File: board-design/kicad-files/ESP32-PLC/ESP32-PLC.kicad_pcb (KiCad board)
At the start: 2 copper layers, 58.1 x 172.1 mm, 80 parts, among them J1 640456-3, J2 Conn_ARM_JTAG_SWD_10, J3 302-S101, J4 302-S101, J5 RJ45_Wuerth_7499010121A, Q1 BC817, Q2 BC817, U1 BD48ExxG, U2 ESP32-WROVER-E, U3 LAN8720A, Y1 Q25MHz/20ppm/3.2x2.5mm (FL250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

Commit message: [UPDATE]
Finished ESP32 and ESP32-programmer board designs (few corrections to be made when manufacturer is chosen - design rules).

Signed-off-by: Nicolae-Andrei Vasile <vasilenicolaeandrei@gmail.com>
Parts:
- added H1: MountingHole, MountingHole:MountingHole_2.5mm_Pad_Via, F.Cu at (73.9, 24.1)
- added H2: MountingHole, MountingHole:MountingHole_2.5mm_Pad_Via, F.Cu at (123.9, 24.1)
- added H3: MountingHole, MountingHole:MountingHole_2.5mm_Pad_Via, F.Cu at (73.9, 186.1)
- added H4: MountingHole, MountingHole:MountingHole_2.5mm_Pad_Via, F.Cu at (123.9, 186.1)
- J4: moved to B.Cu
- moved R19 186.2 mm to (83.8, 144.1)
- moved R20 186.2 mm to (83.8, 145.4)
- moved R13 177.1 mm to (83.8, 153.0)
- moved R14 177.0 mm to (83.8, 154.3)
- moved R15 176.5 mm to (83.8, 151.8)
- moved U2 142.7 mm to (107.6, 63.9), turned to -90 degrees
- moved C6 122.3 mm to (115.6, 52.7), turned to 0 degrees
- moved C7 120.2 mm to (115.6, 50.8), turned to 0 degrees
- moved R1 115.6 mm to (107.3, 47.0), turned to -90 degrees
- moved J4 114.0 mm to (94.0, 24.6), turned to -90 degrees
- moved C8 113.4 mm to (117.5, 47.0), turned to 0 degrees
- moved C24 112.8 mm to (104.8, 138.4)
- moved L3 107.5 mm to (104.8, 136.5)
- moved R5 106.9 mm to (100.8, 42.5), turned to 180 degrees
- moved J3 106.7 mm to (94.0, 87.1), turned to 90 degrees
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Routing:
- net Net-(U3-VDD1A): track 0.00 -> 192.1 mm, vias 0 -> 9
- net +3V3: track 0.00 -> 181.6 mm, vias 0 -> 2
- net /LAN8720A/GPIO26/EMAC_RXD1: track 0.00 -> 151.5 mm, vias 0 -> 2
- net /LAN8720A/GPIO25/EMAC_RXD0: track 0.00 -> 149.6 mm, vias 0 -> 2
- net /GPIO0/REFCLKO: track 0.00 -> 139.7 mm, vias 0 -> 3
- net Net-(Q1-C): track 0.00 -> 137.0 mm, vias 0 -> 2
- net /LAN8720A/GPIO22/EMAC_TXD1: track 0.00 -> 135.2 mm, vias 0 -> 2
- net /LAN8720A/GPIO5/~{RST}: track 0.00 -> 126.0 mm, vias 0 -> 2
- net /LAN8720A/GPIO19/EMAC_TXD0: track 0.00 -> 123.7 mm, vias 0 -> 2
- net /LAN8720A/GPIO27/EMAC_CRS_DV: track 0.00 -> 123.6 mm, vias 0 -> 2
- net /LAN8720A/GPIO23/MDC: track 0.00 -> 122.8 mm, vias 0 -> 2
- net Net-(U1-VDD): track 0.00 -> 120.3 mm, vias 0 -> 2
- net /LAN8720A/GPIO21/EMAC_TXEN: track 0.00 -> 120.2 mm, vias 0 -> 2
- net /LAN8720A/GPIO18/MDIO: track 0.00 -> 107.2 mm, vias 0 -> 2
- net /ESP32_INT: track 0.00 -> 100.1 mm, vias 0 -> 1
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- added copper zone on B.Cu, net Earth_Protective
- added copper zone on F.Cu, net Earth_Protective
- added copper zone on B.Cu, net GND
- added copper zone on F.Cu, net GND

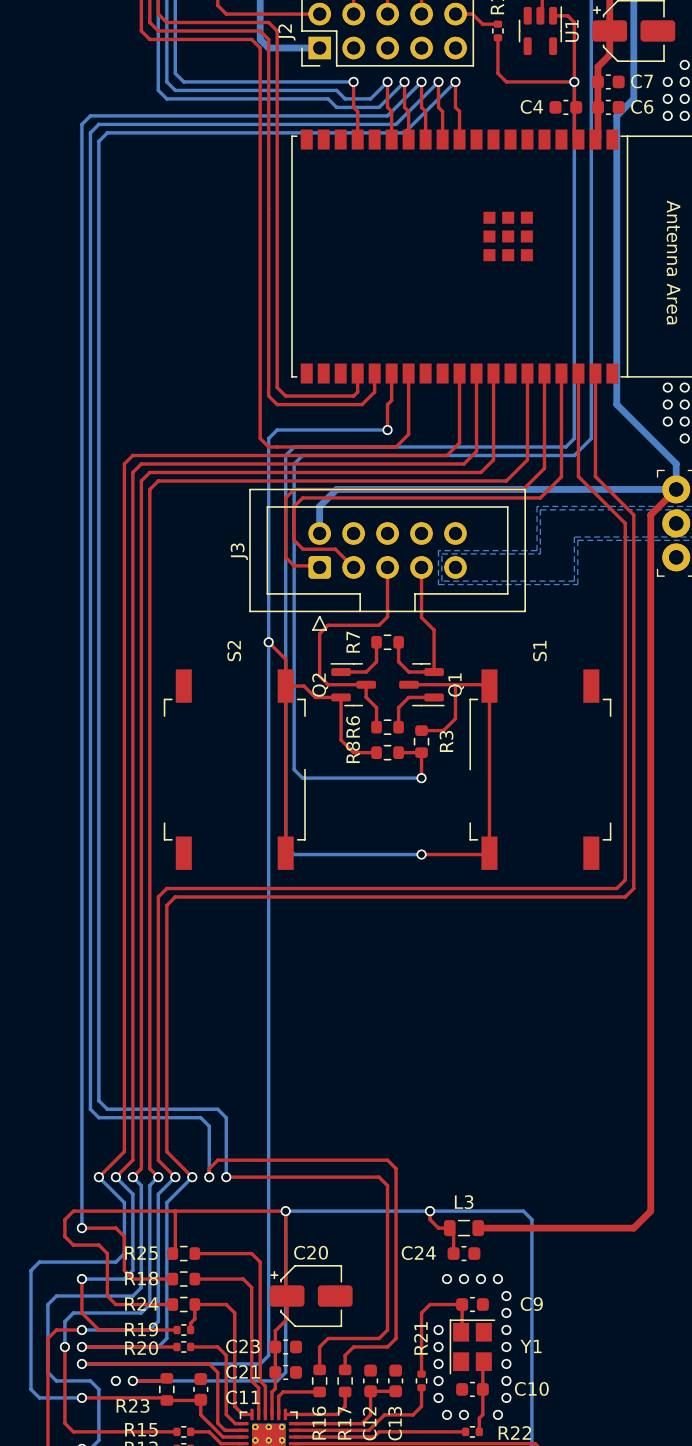
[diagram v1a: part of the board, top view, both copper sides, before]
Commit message: [FIX]
Updated footprints for tactile switches.

Signed-off-by: Nicolae-Andrei Vasile <vasilenicolaeandrei@gmail.com>
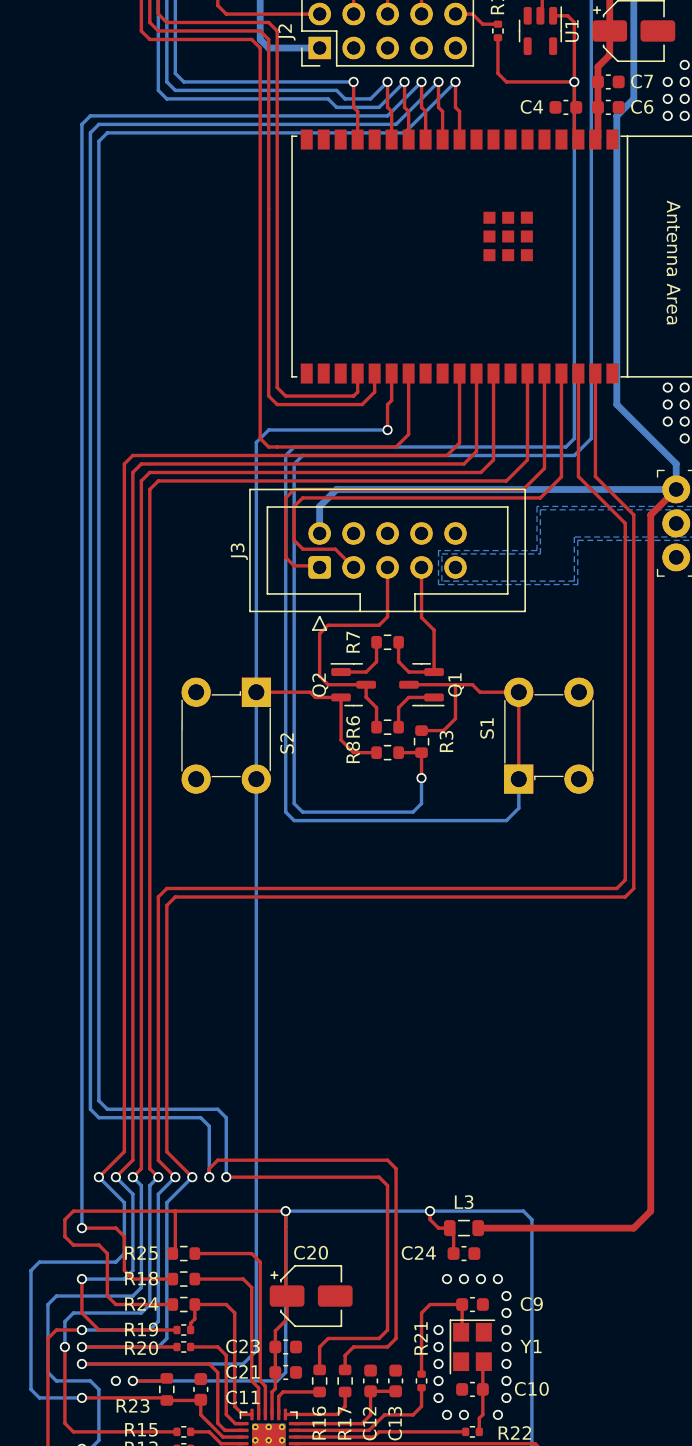
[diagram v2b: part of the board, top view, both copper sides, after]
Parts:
- S1, S2: footprint Button_Switch_SMD:SW_MEC_5GSH9 -> digikey-footprints:Switch_Tactile_THT_6x6mm
- moved S2 6.01 mm to (89.2, 96.4), turned to -90 degrees
- moved S1 1.76 mm to (108.9, 102.9), turned to 90 degrees
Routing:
- net /GPIO0/REFCLKO: track 139.7 -> 125.0 mm, vias 3 -> 2
- net Net-(U1-VDD): track 120.3 -> 125.1 mm
- net Net-(Q1-C): track 137.0 -> 135.5 mm, vias 2 -> 1

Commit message: [UPDATE]
Work in progress.

Signed-off-by: Nicolae-Andrei Vasile <vasilenicolaeandrei@gmail.com>
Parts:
- added BT1: CR2032 (Panasonic vertical), Battery:Battery_Panasonic_CR2032-VS1N_Vertical_CircularHoles, F.Cu at (96.8, 243.7)
- added C25: 0.1uF/6.3V/20%/C0603, Capacitor_SMD:C_0603_1608Metric, F.Cu at (346.7, 293.4)
- added C26: 33pF/6.3V/20%/C0603, Capacitor_SMD:C_0603_1608Metric, F.Cu at (339.1, 286.4)
- added C27: 33pF/6.3V/20%/C0603, Capacitor_SMD:C_0603_1608Metric, F.Cu at (339.1, 291.5)
- added C28: 10nF/6.3V/20%/C0603, Capacitor_SMD:C_0603_1608Metric, F.Cu at (346.7, 278.1)
- added C29: 33pF/6.3V/20%/C0603, Capacitor_SMD:C_0603_1608Metric, F.Cu at (342.9, 293.4)
- added C30: 100uF/16V/20%/4x5.4mm, Capacitor_SMD:CP_Elec_4x5.4, F.Cu at (373.4, 234.9)
- added C31: 0.1uF/6.3V/20%/C0603, Capacitor_SMD:C_0603_1608Metric, F.Cu at (371.5, 238.8)
- added C32: 33pF/6.3V/20%/C0603, Capacitor_SMD:C_0603_1608Metric, F.Cu at (371.5, 240.7)
- added C33: 10pF/6.3V/20%/C0603, Capacitor_SMD:C_0603_1608Metric, F.Cu at (371.5, 242.6)
- added C34: 10pF/6.3V/20%/C0603, Capacitor_SMD:C_0603_1608Metric, F.Cu at (368.3, 242.6)
- added C35: 33pF/6.3V/20%/C0603, Capacitor_SMD:C_0603_1608Metric, F.Cu at (368.3, 240.7)
- added C36: 0.1uF/6.3V/20%/C0603, Capacitor_SMD:C_0603_1608Metric, F.Cu at (368.3, 238.8)
- added C37: 100uF/16V/20%/4x5.4mm, Capacitor_SMD:CP_Elec_4x5.4, F.Cu at (366.4, 234.9)
- added C38: 1uF/6.3V/20%/C0603, Capacitor_SMD:C_0603_1608Metric, F.Cu at (347.3, 236.9)
- added C39: 1uF/6.3V/20%/C0603, Capacitor_SMD:C_0603_1608Metric, F.Cu at (339.1, 272.4)
- added C40: 10uF/6.3V/20%/C0603, Capacitor_SMD:C_0603_1608Metric, F.Cu at (349.2, 236.9)
- added C41: 10uF/6.3V/20%/C0603, Capacitor_SMD:C_0603_1608Metric, F.Cu at (339.1, 270.5)
- added C42: 0.1uF/6.3V/20%/C0603, Capacitor_SMD:C_0603_1608Metric, F.Cu at (351.2, 236.9)
- added C43: 0.1uF/6.3V/20%/C0603, Capacitor_SMD:C_0603_1608Metric, F.Cu at (339.1, 268.6)
- added C44: 0.1uF/6.3V/20%/C0603, Capacitor_SMD:C_0603_1608Metric, F.Cu at (349.2, 233.0)
- added C45: 0.1uF/6.3V/20%/C0603, Capacitor_SMD:C_0603_1608Metric, F.Cu at (335.3, 270.5)
- added C46: 10uF/6.3V/20%/C0603, Capacitor_SMD:C_0603_1608Metric, F.Cu at (351.2, 233.0)
- added C47: 10uF/6.3V/20%/C0603, Capacitor_SMD:C_0603_1608Metric, F.Cu at (335.3, 268.6)
- added C48: 22uF/6.3V/20%/C0603, Capacitor_SMD:C_0603_1608Metric, F.Cu at (339.1, 254.0)
- added C49: 22uF/6.3V/20%/C0603, Capacitor_SMD:C_0603_1608Metric, F.Cu at (92.8, 246.9)
- added C50: 0.1uF/6.3V/20%/C0603, Capacitor_SMD:C_0603_1608Metric, F.Cu at (92.8, 249.5)
- added C51: 10uF/16V/20%/4x5.4mm, Capacitor_SMD:CP_Elec_4x5.4, F.Cu at (107.2, 248.6)
- added C52: 0.1uF/6.3V/20%/C0603, Capacitor_SMD:C_0603_1608Metric, F.Cu at (92.8, 252.0)
- added C53: 10pF/6.3V/10%/C0603, Capacitor_SMD:C_0603_1608Metric, F.Cu at (92.8, 254.5)
- added C54: 10pF/6.3V/10%/C0603, Capacitor_SMD:C_0603_1608Metric, F.Cu at (92.8, 257.0)
- added C55: 0.1uF/6.3V/20%/C0603, Capacitor_SMD:C_0603_1608Metric, F.Cu at (92.8, 259.5)
- added C56: 10uF/16V/20%/4x5.4mm, Capacitor_SMD:CP_Elec_4x5.4, F.Cu at (107.2, 254.5)
- added D1: ESDA6V1-5SC6, Package_TO_SOT_SMD:SOT-23-6, F.Cu at (342.9, 288.9)
- added D2: VESD05C1-02V, Diode_SMD:D_SOD-523, F.Cu at (373.4, 229.2)
- added D3: 20V/0.5A/0.5V (NSR0620P2T5G), Diode_SMD:D_SOD-923, F.Cu at (101.3, 259.6)
- added J6: RJ45_Wuerth_7499010121A, Connector_RJ:RJ45_Wuerth_7499010121A_Horizontal, F.Cu at (365.2, 55.6)
- added J7: SF53S006VCBR2000, Connector_Card:microSIM_JAE_SF53S006VCBR2000, F.Cu at (355.6, 287.7)
- added L4: FB0805/600R/2A, Inductor_SMD:L_0805_2012Metric, F.Cu at (371.5, 229.2)
- added L5: FB0805/600R/2A, Inductor_SMD:L_0805_2012Metric, F.Cu at (347.3, 233.0)
- added L6: FB0805/600R/2A, Inductor_SMD:L_0805_2012Metric, F.Cu at (335.3, 272.4)
- added L7: FB0805/600R/2A, Inductor_SMD:L_0805_2012Metric, F.Cu at (105.6, 258.8)
- added L8: FB0805/600R/2A, Inductor_SMD:L_0805_2012Metric, F.Cu at (105.6, 261.5)
- added Q3: BC817, Package_TO_SOT_SMD:SOT-23, F.Cu at (342.9, 279.4)
- added Q4: BC817, Package_TO_SOT_SMD:SOT-23, F.Cu at (342.9, 283.2)
- added R35: 4.7K/R0603, Resistor_SMD:R_0603_1608Metric, F.Cu at (339.1, 278.1)
- added R36: 4.7K/R0603, Resistor_SMD:R_0603_1608Metric, F.Cu at (339.1, 282.6)
- added R37: 47K/R0603, Resistor_SMD:R_0603_1608Metric, F.Cu at (339.1, 280.0)
- added R38: 47K/R0603, Resistor_SMD:R_0603_1608Metric, F.Cu at (339.1, 284.5)
- added R39: 15K/R0603, Resistor_SMD:R_0603_1608Metric, F.Cu at (344.8, 293.4)
- added R40: 0R(board_mounted), Resistor_SMD:R_0402_1005Metric, F.Cu at (339.1, 288.3)
- added R41: 0R(board_mounted), Resistor_SMD:R_0402_1005Metric, F.Cu at (339.1, 289.6)
- added R42: 0R(board_mounted), Resistor_SMD:R_0402_1005Metric, F.Cu at (341.0, 293.4)
- added R43: 10K/R0603, Resistor_SMD:R_0603_1608Metric, F.Cu at (360.0, 236.9)
- added R44: 120K/R0603, Resistor_SMD:R_0603_1608Metric, F.Cu at (361.9, 236.9)
- added R45: 10K/R0603, Resistor_SMD:R_0603_1608Metric, F.Cu at (339.1, 259.7)
- added R46: 120K/R0603, Resistor_SMD:R_0603_1608Metric, F.Cu at (339.1, 257.8)
- added R47: 51K/R0603, Resistor_SMD:R_0603_1608Metric, F.Cu at (339.1, 255.9)
- added R48: 0R(board_mounted), Resistor_SMD:R_0402_1005Metric, F.Cu at (351.2, 226.7)
- added R49: 0R(board_mounted), Resistor_SMD:R_0402_1005Metric, F.Cu at (352.4, 226.7)
- added R50: 0R(board_mounted), Resistor_SMD:R_0402_1005Metric, F.Cu at (353.7, 226.7)
- added R51: 0R(board_mounted), Resistor_SMD:R_0402_1005Metric, F.Cu at (355.0, 226.7)
- added R52: 0R(board_mounted), Resistor_SMD:R_0402_1005Metric, F.Cu at (356.2, 226.7)
- added R53: 0R(board_mounted), Resistor_SMD:R_0402_1005Metric, F.Cu at (357.5, 226.7)
- added R54: 0R(board_mounted), Resistor_SMD:R_0402_1005Metric, F.Cu at (358.8, 226.7)
- added R55: 0R(board_mounted), Resistor_SMD:R_0402_1005Metric, F.Cu at (360.0, 226.7)
- added R56: 51K/R0603, Resistor_SMD:R_0603_1608Metric, F.Cu at (335.3, 259.7)
- added R57: 10K/R0603, Resistor_SMD:R_0603_1608Metric, F.Cu at (339.1, 252.1)
- added R58: 0R(board_mounted), Resistor_SMD:R_0402_1005Metric, F.Cu at (334.6, 255.9)
- added R59: 0R(board_mounted), Resistor_SMD:R_0402_1005Metric, F.Cu at (334.6, 257.2)
- added R60: 10K/R0603, Resistor_SMD:R_0603_1608Metric, F.Cu at (92.8, 262.0)
- added R61: 10K/R0603, Resistor_SMD:R_0603_1608Metric, F.Cu at (92.8, 264.5)
- added RV2: V5.5MLA0603N, Resistor_SMD:R_0603_1608Metric, F.Cu at (351.2, 302.3)
- added U4: EC21, my_RF_LTE:Quectel_EC21_L29.0mm_W32.0mm, F.Cu at (361.9, 260.4)
- added U5: TXS0108EPW, Package_SO:TSSOP-20_4.4x6.5mm_P0.65mm, F.Cu at (355.6, 234.9)
- added U6: TXS0108EPW, Package_SO:TSSOP-20_4.4x6.5mm_P0.65mm, F.Cu at (337.2, 264.2)
- added U7: MCP7940N-xSN, Package_SO:SOIC-8_3.9x4.9mm_P1.27mm, F.Cu at (99.1, 248.9)
- added U8: 24LC512, Package_SO:SOIC-8_3.9x4.9mm_P1.27mm, F.Cu at (99.1, 255.4)
- added XTAL1: ECS-_327-7-34B-TR, digikey-footprints:SMD-2_3.2x1.5mm, F.Cu at (97.4, 260.3)
- C4: value 1uF/6.3V/20%/C0603 -> 0.1uF/6.3V/20%/C0603
- C5: value 22uF/6.3V/20%/C0603 -> 1uF/6.3V/20%/C0603
- C6: value 0.1uF/6.3V/20%/C0603 -> 22uF/16V/20%/4.3x4.3mm; footprint Capacitor_SMD:C_0603_1608Metric -> Capacitor_SMD:CP_Elec_4x5.4
- C7: value 1uF/6.3V/20%/C0603 -> 22uF/6.3V/20%/C0603
- C8: value 22uF/16V/20%/4.3x4.3mm -> 1uF/6.3V/20%/C0603; footprint Capacitor_SMD:CP_Elec_4x5.4 -> Capacitor_SMD:C_0603_1608Metric
- J4: value 302-S101 -> Conn_02x05_Odd_Even
- J5: value RJ45_Wuerth_7499010121A -> Conn_02x10_Odd_Even; footprint Connector_RJ:RJ45_Wuerth_7499010121A_Horizontal -> Connector_IDC:IDC-Header_2x10_P2.54mm_Vertical; moved to B.Cu
- R3: value 10K/R0603 -> 100K/R0603
- R5: value 100K/R0603 -> 10K/R0603
- moved JP1 331.8 mm to (417.2, 95.2), turned to 0 degrees
- moved R13 320.2 mm to (387.4, 51.3)
- moved R14 319.9 mm to (387.4, 53.3)
- moved R15 318.5 mm to (387.4, 55.3)
- moved R19 315.8 mm to (387.4, 57.2)
- moved R20 315.6 mm to (387.4, 59.2)
- moved R31 307.1 mm to (387.4, 65.2), turned to 0 degrees
- moved U3 305.8 mm to (385.4, 73.0), turned to 0 degrees
- moved C17 304.9 mm to (378.4, 78.7), turned to 0 degrees
- moved R21 298.7 mm to (387.4, 61.2), turned to 0 degrees
- moved R23 296.3 mm to (368.5, 71.1), turned to 0 degrees
- moved R22 295.6 mm to (387.4, 63.2), turned to 0 degrees
- moved R24 292.9 mm to (368.5, 73.6), turned to 0 degrees
- moved RV1 292.9 mm to (372.5, 78.7), turned to 0 degrees
- moved R25 291.4 mm to (368.5, 76.2), turned to 0 degrees
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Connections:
- C22 pad 1: Net-(J5-RCT) -> Net-(J6-RCT)
- C3 pad 1: Net-(U1-VDD) -> Net-(J2-VTref)
- C4 pad 1: Net-(Q1-C) -> Net-(J2-VTref)
- C7 pad 1: Net-(J2-VTref) -> Net-(U1-VDD)
- C8 pad 1: Net-(J2-VTref) -> Net-(Q1-C)
- J4 pad 1: Net-(J4-Pad1) -> +3V3
- J4 pad 10: GND -> Net-(J4-Pin_10)
- J4 pad 3: Earth_Protective -> /SAM4E_INT
- J4 pad 4: /ESP32_INT -> Net-(J4-Pin_4)
- J4 pad 5: Net-(J4-Pad5) -> /ESP32_INT
- J4 pad 6: /SAM4E_INT -> Net-(J4-Pin_6)
- J4 pad 7: Net-(J4-Pad7) -> GND
- J4 pad 8: GND -> Net-(J4-Pin_8)
- J4 pad 9: Net-(J4-Pad9) -> GND
- J5 pad 1: Net-(J5-TD+) -> /LTE/LTE_UART_DBG_TXD
- J5 pad 10: Net-(U3-LED1/REGOFF) -> /LTE_UART_RXD
- J5 pad 11: Net-(J5-Pad11) -> /LTE/LTE_AP_READY
- J5 pad 12: Net-(U3-LED2/~{INTSEL}) -> /LTE_UART_TXD
- J5 pad 2: Net-(J5-RCT) -> /LTE_UART_DCD
- J5 pad 3: Net-(J5-TD-) -> /LTE/LTE_UART_DTR
- J5 pad 4: Net-(J5-RD+) -> /LTE_UART_CTS
- J5 pad 5: Net-(J5-RCT) -> /LTE/LTE_UART_DBG_RXD
- J5 pad 6: Net-(J5-RD-) -> /LTE_UART_RI
- J5 pad 7: unconnected-(J5-NC-Pad7) -> /RTC_EEPROM/SCL
- J5 pad 8: GND -> /LTE_UART_RTS
- J5 pad 9: Net-(J5-Pad9) -> /RTC_EEPROM/SDA
- JP2 pad 1: /MOSI -> /CS0
- JP2 pad 2: /GPIO13 -> /GPIO15
- JP2 pad 3: /MTCK -> /MTDO
- JP3 pad 1: /CS0 -> /MISO
- JP3 pad 2: /GPIO15 -> /GPIO12
- JP3 pad 3: /MTDO -> /MTDI
- JP5 pad 1: /MISO -> /MOSI
- JP5 pad 2: /GPIO12 -> /GPIO13
- JP5 pad 3: /MTDI -> /MTCK
- R10 pad 1: /CS0 -> /MISO
- R10 pad 2: Net-(J4-Pad5) -> Net-(J4-Pin_6)
- R11 pad 2: Net-(J4-Pad7) -> Net-(J4-Pin_8)
- R12 pad 1: /MISO -> /MOSI
- R12 pad 2: Net-(J4-Pad9) -> Net-(J4-Pin_10)
- R27 pad 1: Net-(J5-RD-) -> Net-(J6-RD-)
- R28 pad 1: Net-(J5-RD+) -> Net-(J6-RD+)
- R29 pad 1: Net-(J5-TD-) -> Net-(J6-TD-)
- R3 pad 1: Net-(Q1-C) -> /MTMS
- R3 pad 2: Net-(U1-VDD) -> Net-(J2-VTref)
- R30 pad 1: Net-(J5-TD+) -> Net-(J6-TD+)
- R31 pad 1: Net-(J5-RCT) -> Net-(J6-RCT)
- R32 pad 1: Net-(J5-Pad11) -> Net-(J6-Pad11)
- R33 pad 1: Net-(J5-Pad9) -> Net-(J6-Pad9)
- R4 pad 1: /MTMS -> /MTDI
- R5 pad 1: /MTDI -> Net-(Q1-C)
- R5 pad 2: Net-(J2-VTref) -> Net-(U1-VDD)
- R9 pad 1: /MOSI -> /CS0
- R9 pad 2: Net-(J4-Pad1) -> Net-(J4-Pin_4)
- U3 pad 20: Net-(J5-TD-) -> Net-(J6-TD-)
- U3 pad 21: Net-(J5-TD+) -> Net-(J6-TD+)
- U3 pad 22: Net-(J5-RD-) -> Net-(J6-RD-)
- U3 pad 23: Net-(J5-RD+) -> Net-(J6-RD+)
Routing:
- net Net-(U3-VDD1A): track 192.1 -> 0.00 mm, vias 9 -> 0
- net +3V3: track 181.6 -> 26.1 mm, vias 2 -> 0
- net /LAN8720A/GPIO26/EMAC_RXD1: track 151.5 -> 2.62 mm, vias 2 -> 1
- net /LAN8720A/GPIO25/EMAC_RXD0: track 149.6 -> 2.62 mm, vias 2 -> 1
- net /LAN8720A/GPIO22/EMAC_TXD1: track 135.2 -> 2.07 mm, vias 2 -> 1
- net /LAN8720A/GPIO5/~{RST}: track 126.0 -> 2.07 mm, vias 2 -> 1
- net /LAN8720A/GPIO19/EMAC_TXD0: track 123.7 -> 2.07 mm, vias 2 -> 1
- net /LAN8720A/GPIO27/EMAC_CRS_DV: track 123.6 -> 2.62 mm, vias 2 -> 1
- net /LAN8720A/GPIO23/MDC: track 122.8 -> 2.07 mm, vias 2 -> 1
- net /LAN8720A/GPIO21/EMAC_TXEN: track 120.2 -> 2.07 mm, vias 2 -> 1
- net /GPIO0/REFCLKO: track 125.0 -> 16.2 mm, vias 2 -> 1
- net Net-(U1-VDD): track 125.1 -> 20.0 mm, vias 2 -> 0
- net /LAN8720A/GPIO18/MDIO: track 107.2 -> 2.07 mm, vias 2 -> 1
- net /ESP32_INT: track 100.1 -> 5.02 mm, vias 1 -> 2
- net /SAM4E_INT: track 95.9 -> 7.04 mm, vias 1 -> 2
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- removed copper zone on B.Cu, net Earth_Protective
- removed copper zone on F.Cu, net Earth_Protective
- removed copper zone on B.Cu, net GND
- removed copper zone on F.Cu, net GND

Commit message: [UPDATE]
Finished ESP32-PLC board design

Signed-off-by: Nicolae-Andrei Vasile <vasilenicolaeandrei@gmail.com>
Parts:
- removed C55: 0.1uF/6.3V/20%/C0603, Capacitor_SMD:C_0603_1608Metric
- removed C56: 10uF/16V/20%/4x5.4mm, Capacitor_SMD:CP_Elec_4x5.4
- removed L8: FB0805/600R/2A, Inductor_SMD:L_0805_2012Metric
- removed U8: 24LC512, Package_SO:SOIC-8_3.9x4.9mm_P1.27mm
- moved RV2 315.2 mm to (127.6, 80.0), turned to 180 degrees
- moved Q4 310.2 mm to (108.0, 80.6)
- moved R36 310.2 mm to (104.1, 80.0)
- moved R38 310.2 mm to (104.1, 81.9)
- moved R58 308.2 mm to (99.1, 57.1)
- moved R59 308.2 mm to (99.1, 58.4)
- moved R56 308.2 mm to (99.7, 61.0)
- moved C31 307.7 mm to (136.5, 40.0)
- moved C32 307.7 mm to (136.5, 41.9)
- moved C33 307.7 mm to (136.5, 43.8)
- moved C34 307.7 mm to (133.3, 43.8)
- moved C35 307.7 mm to (133.3, 41.9)
- moved C36 307.7 mm to (133.3, 40.0)
- moved C38 307.7 mm to (112.4, 38.1)
- moved J7 307.7 mm to (120.7, 88.9)
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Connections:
- net /RTC_EEPROM/RTC_MFP renamed /RTC/RTC_MFP
- net /RTC_EEPROM/SCL renamed /RTC/SCL
- net /RTC_EEPROM/SDA renamed /RTC/SDA
- J1 pad 1: GND -> Earth_Protective
- J1 pad 2: Earth_Protective -> GND
- J7 pad SH: Net-(J7-PadSH) -> Earth_Protective
- RV2 pad 2: Net-(J7-PadSH) -> Earth_Protective
- U4 pad 114: unconnected-(U4-RESERVED-Pad113) -> unconnected-(U4-RESERVED-Pad114)
- U4 pad 116: unconnected-(U4-RESERVED-Pad113) -> unconnected-(U4-RESERVED-Pad116)
- U4 pad 117: unconnected-(U4-RESERVED-Pad113) -> unconnected-(U4-RESERVED-Pad117)
- U4 pad 140: unconnected-(U4-RESERVED-Pad113) -> unconnected-(U4-RESERVED-Pad140)
- U4 pad 141: unconnected-(U4-RESERVED-Pad113) -> unconnected-(U4-RESERVED-Pad141)
- U4 pad 142: unconnected-(U4-RESERVED-Pad113) -> unconnected-(U4-RESERVED-Pad142)
- U4 pad 143: unconnected-(U4-RESERVED-Pad113) -> unconnected-(U4-RESERVED-Pad143)
- U4 pad 144: unconnected-(U4-RESERVED-Pad113) -> unconnected-(U4-RESERVED-Pad144)
- U4 pad 18: unconnected-(U4-RESERVED-Pad113) -> unconnected-(U4-RESERVED-Pad18)
- U4 pad 3: unconnected-(U4-RESERVED-Pad113) -> unconnected-(U4-RESERVED-Pad3)
- U4 pad 43: unconnected-(U4-RESERVED-Pad113) -> unconnected-(U4-RESERVED-Pad43)
- U4 pad 55: unconnected-(U4-RESERVED-Pad113) -> unconnected-(U4-RESERVED-Pad55)
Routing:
- net +3V3: track 26.1 -> 451.8 mm
- net /RTC/RTC_MFP: track 0.00 -> 185.0 mm, vias 0 -> 1
- net Net-(U3-VDD1A): track 0.00 -> 139.1 mm, vias 0 -> 11
- net /ESP32_INT: track 5.02 -> 100.8 mm
- net /RTC/SDA: track 50.3 -> 143.4 mm, vias 0 -> 1
- net /SAM4E_INT: track 7.04 -> 99.7 mm
- net /RTC/SCL: track 47.5 -> 139.0 mm, vias 0 -> 1
- net /GPIO0/REFCLKO: track 16.2 -> 90.2 mm, vias 1 -> 2
- net /U0RXD: track 2.07 -> 68.9 mm
- net /LAN8720A/GPIO26/EMAC_RXD1: track 2.62 -> 67.1 mm, vias 1 -> 2
- net /U0TXD: track 2.07 -> 62.2 mm
- net /LAN8720A/GPIO25/EMAC_RXD0: track 2.62 -> 59.1 mm, vias 1 -> 2
- net Net-(J6-TD-): track 0.00 -> 55.2 mm
- net /LTE/VDD_EXT: track 27.2 -> 79.8 mm, vias 0 -> 3
- net /LTE/STATUS: track 11.2 -> 57.4 mm, vias 1 -> 2
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- added copper zone on B.Cu, net Earth_Protective
- added copper zone on F.Cu, net Earth_Protective
- added copper zone on B.Cu, net GND
- added copper zone on F.Cu, net GND

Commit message: [Final report]
Added 3D models.

Signed-off-by: Nicolae-Andrei Vasile <vasilenicolaeandrei@gmail.com>
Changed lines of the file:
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@@
     (pad "4" thru_hole circle locked (at 6.5 4.5 90) (size 2.2 2.2) (drill 1.2) (layers "*.Cu" "*.Mask")
       (net 2 "GND") (pintype "passive"))
+    (model "${KIPRJMOD}/1825910_6.3dshapes/1825910-6.step"
+      (offset (xyz 3.302 -2.286 0))
+      (scale (xyz 1 1 1))
+      (rotate (xyz -90 0 0))
+    )
   )
   (footprint "Inductor_SMD:L_0805_2012Metric" locked (layer "F.Cu")
@@
     (pad "24" smd roundrect locked (at -1.25 -1.9375 270) (size 0.25 0.875) (layers "F.Cu" "F.Paste" "F.Mask") (roundrect_rratio 0.25)
       (net 105 "Net-(U3-RBIAS)") (pinfunction "RBIAS") (pintype "passive"))
-    (pad "25" thru_hole circle locked (at -1 -1 270) (size 0.5 0.5) (drill 0.2) (layers "*.Cu")
+    (pad "25" thru_hole circle locked (at -1 -1 270) (size 0.5 0.5) (drill 0.254) (layers "*.Cu")
       (net 2 "GND") (pinfunction "VSS") (pintype "power_in"))
-    (pad "25" thru_hole circle locked (at -1 0 270) (size 0.5 0.5) (drill 0.2) (layers "*.Cu")
+    (pad "25" thru_hole circle locked (at -1 0 270) (size 0.5 0.5) (drill 0.254) (layers "*.Cu")
       (net 2 "GND") (pinfunction "VSS") (pintype "power_in"))
-    (pad "25" thru_hole circle locked (at -1 1 270) (size 0.5 0.5) (drill 0.2) (layers "*.Cu")
+    (pad "25" thru_hole circle locked (at -1 1 270) (size 0.5 0.5) (drill 0.254) (layers "*.Cu")
       (net 2 "GND") (pinfunction "VSS") (pintype "power_in"))
-    (pad "25" thru_hole circle locked (at 0 -1 270) (size 0.5 0.5) (drill 0.2) (layers "*.Cu")
+    (pad "25" thru_hole circle locked (at 0 -1 270) (size 0.5 0.5) (drill 0.254) (layers "*.Cu")
       (net 2 "GND") (pinfunction "VSS") (pintype "power_in"))
-    (pad "25" thru_hole circle locked (at 0 0 270) (size 0.5 0.5) (drill 0.2) (layers "*.Cu")
+    (pad "25" thru_hole circle locked (at 0 0 270) (size 0.5 0.5) (drill 0.254) (layers "*.Cu")
       (net 2 "GND") (pinfunction "VSS") (pintype "power_in"))
     (pad "25" smd rect locked (at 0 0 270) (size 2.5 2.5) (layers "F.Cu" "F.Mask")
@@
     (pad "25" smd rect locked (at 0 0 270) (size 2.5 2.5) (layers "B.Cu")
       (net 2 "GND") (pinfunction "VSS") (pintype "power_in"))
-    (pad "25" thru_hole circle locked (at 0 1 270) (size 0.5 0.5) (drill 0.2) (layers "*.Cu")
+    (pad "25" thru_hole circle locked (at 0 1 270) (size 0.5 0.5) (drill 0.254) (layers "*.Cu")
       (net 2 "GND") (pinfunction "VSS") (pintype "power_in"))
-    (pad "25" thru_hole circle locked (at 1 -1 270) (size 0.5 0.5) (drill 0.2) (layers "*.Cu")
+    (pad "25" thru_hole circle locked (at 1 -1 270) (size 0.5 0.5) (drill 0.254) (layers "*.Cu")
       (net 2 "GND") (pinfunction "VSS") (pintype "power_in"))
-    (pad "25" thru_hole circle locked (at 1 0 270) (size 0.5 0.5) (drill 0.2) (layers "*.Cu")
+    (pad "25" thru_hole circle locked (at 1 0 270) (size 0.5 0.5) (drill 0.254) (layers "*.Cu")
       (net 2 "GND") (pinfunction "VSS") (pintype "power_in"))
-    (pad "25" thru_hole circle locked (at 1 1 270) (size 0.5 0.5) (drill 0.2) (layers "*.Cu")
+    (pad "25" thru_hole circle locked (at 1 1 270) (size 0.5 0.5) (drill 0.254) (layers "*.Cu")
       (net 2 "GND") (pinfunction "VSS") (pintype "power_in"))
     (model "${KICAD6_3DMODEL_DIR}/Package_DFN_QFN.3dshapes/VQFN-24-1EP_4x4mm_P0.5mm_EP2.5x2.5mm.wrl"
@@
     (pad "SH" thru_hole circle locked (at 5.84 12.345 90) (size 2.2 2.2) (drill 1.6) (layers "*.Cu" "*.Mask")
       (net 29 "Earth_Protective") (pintype "passive"))
-    (model "${KICAD6_3DMODEL_DIR}/Connector_RJ.3dshapes/RJ45_Wuerth_7499010121A_Horizontal.wrl"
-      (offset (xyz 0 0 0))
+    (model "${KIPRJMOD}/7499010121A.3dshapes/7499010121A.STEP"
+      (offset (xyz 7.366 -4.572 7.112))
       (scale (xyz 1 1 1))
-      (rotate (xyz 0 0 0))
+      (rotate (xyz 0 0 -90))
     )
   )
@@
       )
     )
+    (model "${KIPRJMOD}/EC21.3dshapes/EC21AFA-512-STD.step"
+      (offset (xyz 0 0 0))
+      (scale (xyz 1 1 1))
+      (rotate (xyz -90 0 0))
+    )
   )
   (footprint "Package_TO_SOT_SMD:SOT-23" locked (layer "F.Cu")
@@
       )
     )
-    (model "${KICAD7_3RD_PARTY}/3dmodels/com_github_espressif_kicad-libraries/espressif.3dshapes/ESP32-WROVER-E.STEP"
-      (offset (xyz -9 -15.7 0))
+    (model "${KIPRJMOD}/ESP32_WROVER_E.3dshapes/ESP32-WROVER-E-N4R8.step"
+      (offset (xyz 0 0 0))
       (scale (xyz 1 1 1))
-      (rotate (xyz 0 0 0))
+      (rotate (xyz -90 0 0))
     )
   )
@@
     (pad "4" thru_hole circle locked (at 6.5 4.5 270) (size 2.2 2.2) (drill 1.2) (layers "*.Cu" "*.Mask")
       (net 2 "GND") (pintype "passive"))
+    (model "${KIPRJMOD}/1825910_6.3dshapes/1825910-6.step"
+      (offset (xyz 3.302 -2.286 0))
+      (scale (xyz 1 1 1))
+      (rotate (xyz -90 0 0))
+    )
   )
   (footprint "Capacitor_SMD:C_0603_1608Metric" locked (layer "F.Cu")
